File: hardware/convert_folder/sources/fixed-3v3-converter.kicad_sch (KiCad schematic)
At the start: 9 parts

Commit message: fix: start fixing the power converters of the board
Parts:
- removed D3: IR26-21C_L110_TR8, LED_SMD:LED_1206_3216Metric, symbol LED:IR26-21C_L110_TR8
- removed R12: RMCF0603FT3K57, altium_import:R0603_MD, symbol altium_import:root_0_RMCF0603FT3K57_Resistor.SchLib
- added LED1: LTST-C190GKT, LEDC1608X90N, symbol lib:LTST-C190GKT
- added Q1: BSS138, SOT95P240X120-3N, symbol lib:BSS138
- added R9: 1K, RESC1608X55N, symbol lib:CRCW06031K00FKEAHP
- 3: value (none) -> ~
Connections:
- net GND: now also Q1.2 (S)
- net V_{IN}: now also R9.1
- net PG_CARRIER: now reaches 3.9 (PG)
- net PG_CARRIER: now also Q1.1 (G)
- net +5V renamed VCCIO_EN
- new net: LED1.2 (A), R9.2
- new net: LED1.1 (K), Q1.3 (D)
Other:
- moved on the sheet: C10, C31

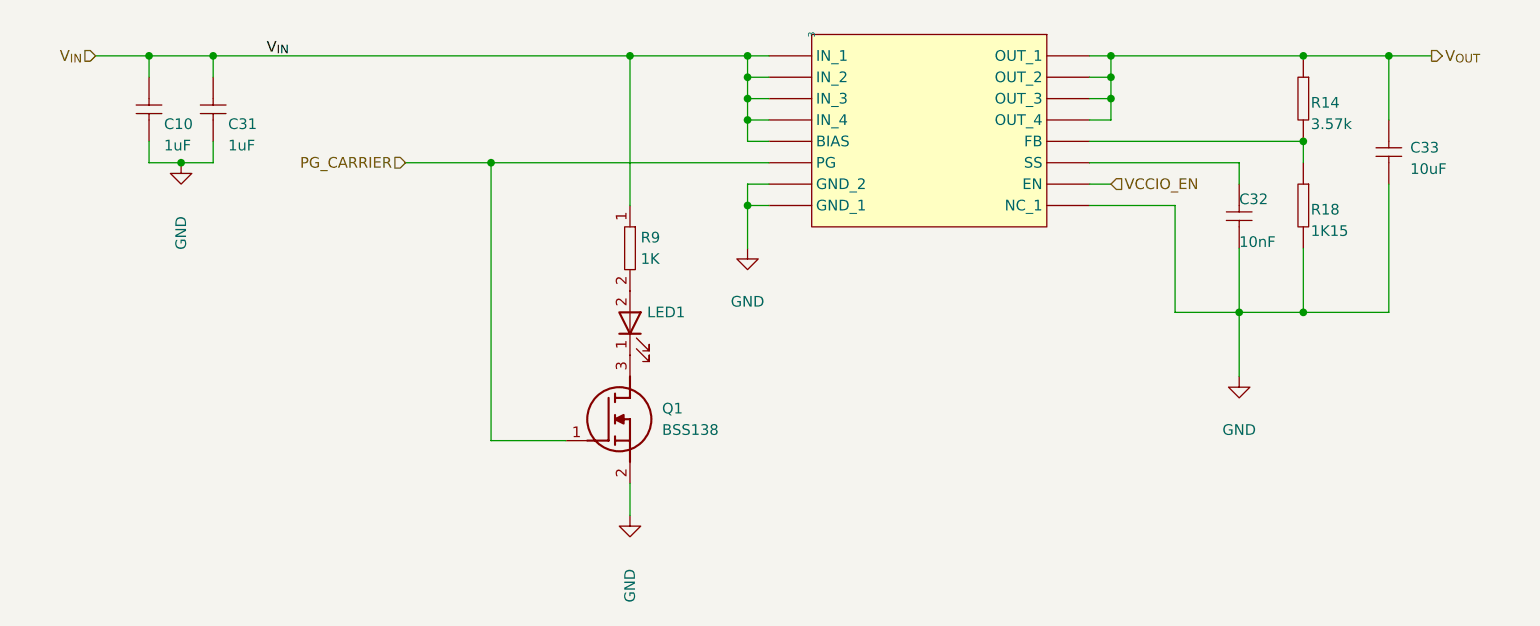
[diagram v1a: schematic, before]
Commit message: fix: add more fixes to the power converters, add resets and other minor corrections
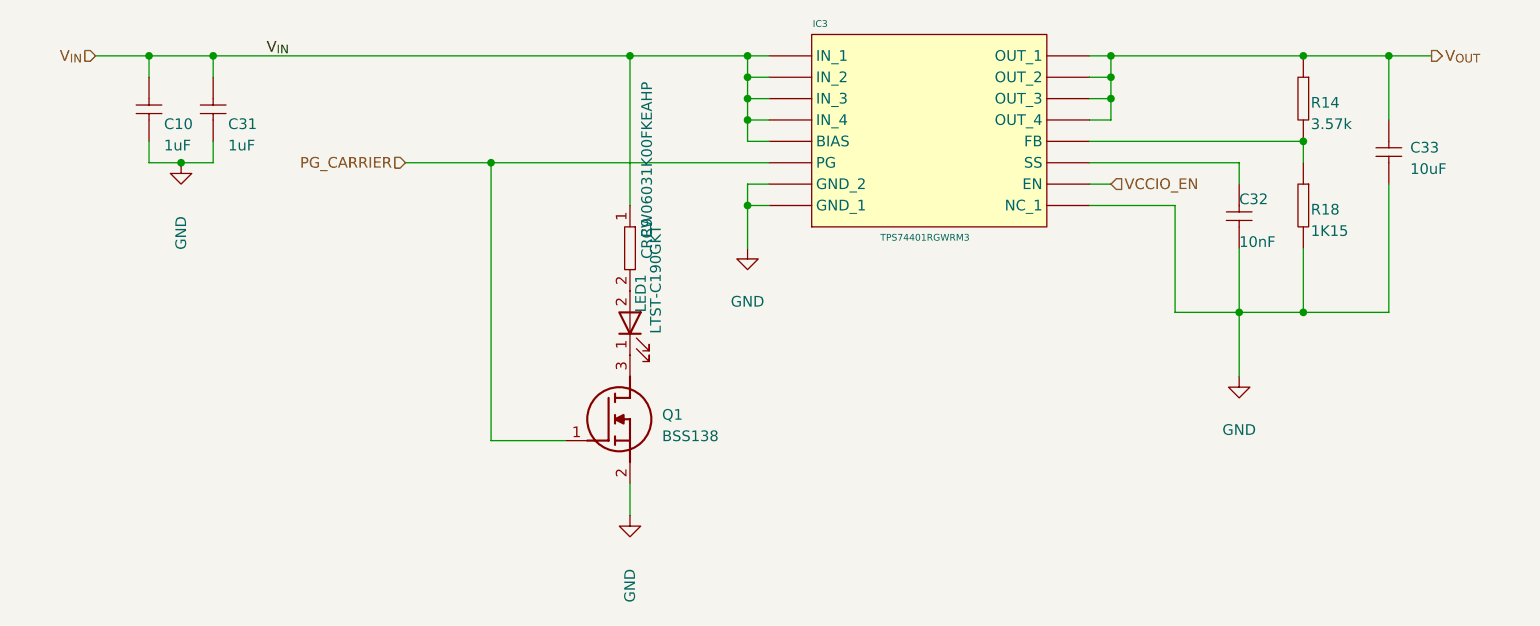
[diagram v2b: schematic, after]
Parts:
- IC3: renamed from 3; value ~ -> TPS74401RGWRM3
- LED1: footprint LEDC1608X90N -> lib:LTST-C190GKT
- Q1: footprint SOT95P240X120-3N -> lib:BSS138
- R9: value 1K -> CRCW06031K00FKEAHP; footprint RESC1608X55N -> lib:CRCW06031K00FKEAHP
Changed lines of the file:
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@@
 		(fields_autoplaced yes)
 		(property "Reference" "R9"
-			(at 255.27 213.3599 90)
-			(effects
-				(font
-					(size 1.27 1.27)
-				)
-				(justify right)
-			)
-		)
-		(property "Value" "1K"
-			(at 255.27 215.8999 90)
-			(effects
-				(font
-					(size 1.27 1.27)
-				)
-				(justify right)
-			)
-		)
-		(property "Footprint" "RESC1608X55N"
+			(at 255.27 213.3599 0)
+			(effects
+				(font
+					(size 1.27 1.27)
+				)
+				(justify left top)
+			)
+		)
+		(property "Value" "CRCW06031K00FKEAHP"
+			(at 255.27 215.8999 0)
+			(effects
+				(font
+					(size 1.27 1.27)
+				)
+				(justify left top)
+			)
+		)
+		(property "Footprint" "lib:CRCW06031K00FKEAHP"
 			(at 350.19 209.55 0)
 			(effects
@@
 		(on_board yes)
 		(dnp no)
-		(property "Reference" "3"
-			(at 275.59 189.23 0)
+		(property "Reference" "IC3"
+			(at 276.606 187.96 90)
 			(do_not_autoplace yes)
 			(effects
@@
 			)
 		)
-		(property "Value" "~"
-			(at 275.59 214.63 0)
+		(property "Value" "TPS74401RGWRM3"
+			(at 289.052 213.36 90)
 			(do_not_autoplace yes)
 			(effects
@@
 			(project "flatsat_platform_2"
 				(path "/8c88a7e1-4137-48d7-b926-b5e762e3852f/8386d232-e6d5-4b15-8289-83f2ee4d46fe/aca72eef-01de-4c32-bcdd-ff44395ea3e5"
-					(reference "3")
+					(reference "IC3")
 					(unit 1)
 				)
 				(path "/8c88a7e1-4137-48d7-b926-b5e762e3852f/8386d232-e6d5-4b15-8289-83f2ee4d46fe/fc9eba0f-963f-4b27-b07a-eeaee98e5f24"
-					(reference "2")
+					(reference "IC2")
 					(unit 1)
 				)
@@
 					(size 1.27 1.27)
 				)
-				(justify left)
+				(justify left top)
 			)
 		)
@@
 					(size 1.27 1.27)
 				)
-				(justify left)
-			)
-		)
-		(property "Footprint" "SOT95P240X120-3N"
+				(justify left top)
+			)
+		)
+		(property "Footprint" "lib:BSS138"
 			(at 257.81 336.22 0)
 			(effects
@@
 		(dnp no)
 		(property "Reference" "LED1"
-			(at 256.032 222.25 90)
-			(effects
-				(font
-					(size 1.27 1.27)
-				)
-				(justify right)
+			(at 256.032 222.25 0)
+			(effects
+				(font
+					(size 1.27 1.27)
+				)
+				(justify left bottom)
 			)
 		)
 		(property "Value" "LTST-C190GKT"
-			(at 257.81 224.7899 90)
-			(effects
-				(font
-					(size 1.27 1.27)
-				)
-				(justify right)
-				(hide yes)
-			)
-		)
-		(property "Footprint" "LEDC1608X90N"
+			(at 257.81 224.7899 0)
+			(effects
+				(font
+					(size 1.27 1.27)
+				)
+				(justify left bottom)
+			)
+		)
+		(property "Footprint" "lib:LTST-C190GKT"
 			(at 347.65 218.44 0)
 			(effects

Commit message: fix: fix caps. values, add decoupling capacitors for INAs and other ICs, and add general improvements
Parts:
- C10: value Cin -> UMK107BJ105KA-T
- C31: value Cbias -> UMK107BJ105KA-T
- C33: value Cout -> GRM188C81C106MA73D
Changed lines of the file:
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@@
 			)
 		)
-		(property "Value" "Cout"
+		(property "Value" "GRM188C81C106MA73D"
 			(at 342.392 198.882 90)
 			(effects
@@
 			)
 		)
-		(property "Value" "Cbias"
+		(property "Value" "UMK107BJ105KA-T"
 			(at 213.36 196.85 90)
 			(effects
@@
 			)
 		)
-		(property "Value" "Cin"
+		(property "Value" "UMK107BJ105KA-T"
 			(at 193.294 197.358 90)
 			(effects
